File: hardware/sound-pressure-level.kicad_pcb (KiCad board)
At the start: 2 copper layers, 25 x 25 mm, 33 parts, among them P1 CON-SENSOR2, P2 BOOT, P3 DEBUG, U1 XMC1XXX48, U2 DRILL, U3 DRILL, U4 DRILL, U5 DRILL, U6 ICS-43432, X1 16MHz

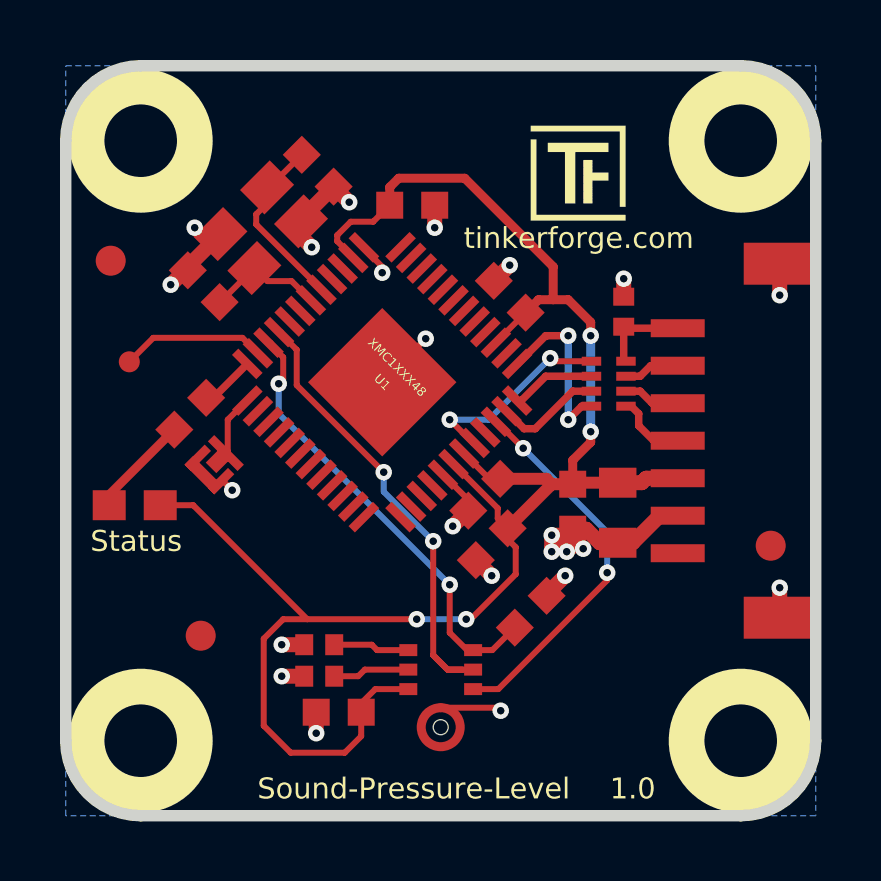
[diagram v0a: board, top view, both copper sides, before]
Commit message: fix logo positions
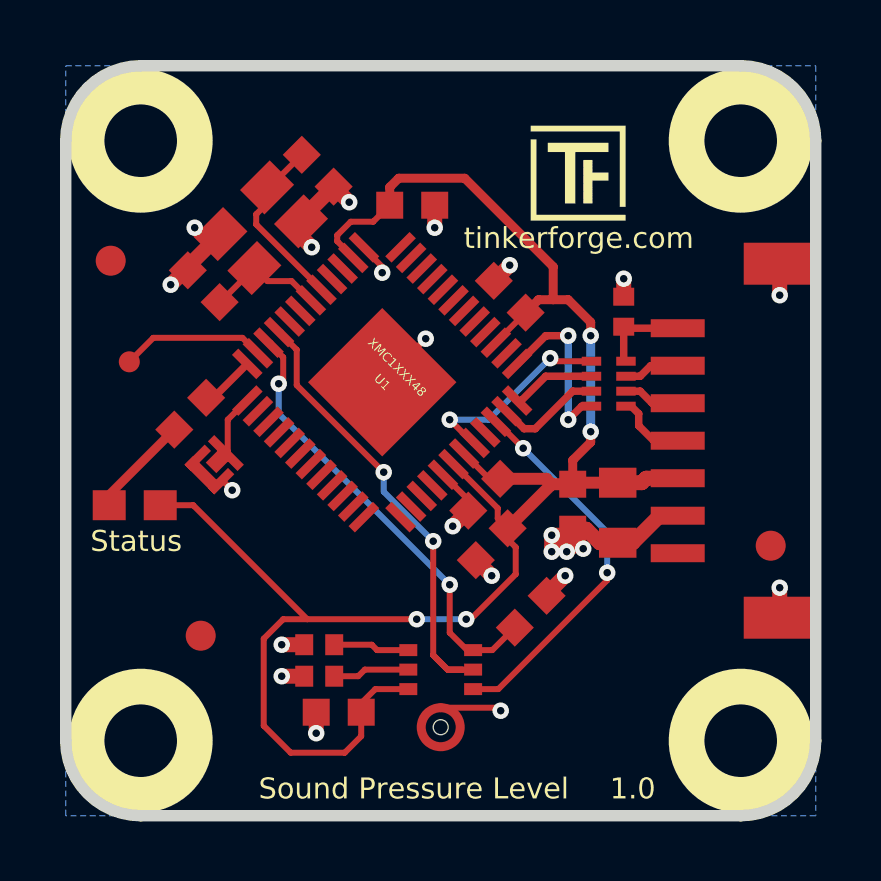
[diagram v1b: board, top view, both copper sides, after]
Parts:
- moved G*** 13.9 mm to (136.4, 141.0)
- moved VAL 8.70 mm to (142.6, 141.0)
- moved VAL 1.30 mm to (148.8, 141.0)
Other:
- board text added: "Sound Pressure Level"
- board text removed: "Sound-Pressure-Level"
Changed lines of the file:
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@@
     (pad_to_mask_clearance 0)
     (aux_axis_origin 0 0)
-    (visible_elements FFFFFF7F)
+    (visible_elements FFFF7F7F)
     (pcbplotparams
       (layerselection 0x00010_00000000)
@@
   )
   (module kicad-libraries:WEEE_7mm (layer B.Cu)
-    (at 133.9 141 180)
+    (at 142.6 141 180)
     (fp_text reference VAL (at 0 0 180) (layer B.SilkS) hide
       (effects (font (size 0.2 0.2) (thickness 0.05)) (justify mirror))
@@
   )
   (module kicad-libraries:CE_5mm (layer B.Cu)
-    (at 150.1 141 180)
+    (at 148.8 141 180)
     (fp_text reference VAL (at 0 0 180) (layer B.SilkS) hide
       (effects (font (size 0.2 0.2) (thickness 0.05)) (justify mirror))
@@
   )
   (module kicad-libraries:Logo_CoMCU (layer B.Cu)
-    (at 147.1 132.15 180)
+    (at 136.4 141 180)
     (fp_text reference G*** (at 0 0 180) (layer B.SilkS) hide
       (effects (font (thickness 0.3)) (justify mirror))
@@
     (effects (font (size 0.7 0.7) (thickness 0.15)))
   )
-  (gr_text Sound-Pressure-Level (at 141.7 152.6) (layer F.SilkS)
+  (gr_text "Sound Pressure Level" (at 141.7 152.6) (layer F.SilkS)
     (effects (font (size 0.7 0.7) (thickness 0.15)))
   )

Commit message: specify processor
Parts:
- U1: value XMC1XXX48 -> XMC1404
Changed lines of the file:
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@@
       (effects (font (size 0.29972 0.29972) (thickness 0.0762)))
     )
-    (fp_text value XMC1XXX48 (at 0 -0.7 315) (layer F.SilkS)
-      (effects (font (size 0.29972 0.29972) (thickness 0.0762)))
+    (fp_text value XMC1404 (at 0 -0.7 315) (layer F.SilkS)
+      (effects (font (size 0.29972 0.29972) (thickness 0.07493)))
     )
     (fp_circle (center -2.5 2.6) (end -2.4 2.8) (layer F.Fab) (width 0.05))
